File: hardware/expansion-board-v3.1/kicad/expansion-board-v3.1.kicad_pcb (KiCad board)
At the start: 6 copper layers, 100 x 62 mm, 156 parts, among them J1 PinHeader_2x20_P2.54mm_Vertic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, J2 U.FL_Hirose_U.FL-R-SMT-1_Vert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, J4 USB_C_Receptacle_HRO_TYPE-C-3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, J5 U.FL_Hirose_U.FL-R-SMT-1_Vert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, J6 U.FL_Hirose_U.FL-R-SMT-1_Vert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, J8 U.FL_Hirose_U.FL-R-SMT-1_Vert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, Q2 SOT-23, Q3 SOT-23, Q4 SOT-23, Q5 SOT-23, SW1 SolderJumper-2_P1.3mm_Open_Pa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, SW2 SolderJumper-2_P1.3mm_Open_Pa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, U1 SOT-23-5, U10 QFN-48-1EP_7x7mm_P0.5mm_EP5.1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, U11 DFN-8-1EP_2x2mm_P0.5mm_EP0.86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, U12 SOT-363_SC-70-6, U13 AD8319_LFCSP-8-EP, U14 MSOP-8_3x3mm_P0.65mm, U15 SOT-23-6, U16 SOT-363_SC-70-6, U17 SOT-363_SC-70-6, U2 SOT-23-5, U3 SOT-23-5, U4 BNO085_LGA-28, U5 BMP388_LGA-10, U6 LGA-16_3x3mm_P0.5mm, U7 ATGM336H_LCC-18, U8 QFN-56-1EP_7x7mm_P0.4mm_EP3.2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, U9 SOIC-8_5.3x5.3mm_P1.27mm, Y1 Crystal_SMD_3225-4Pin_3.2x2.5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, Y2 Crystal_SMD_3225-4Pin_3.2x2.5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, Y3 Crystal_SMD_3215-2Pin_3.2x1.5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

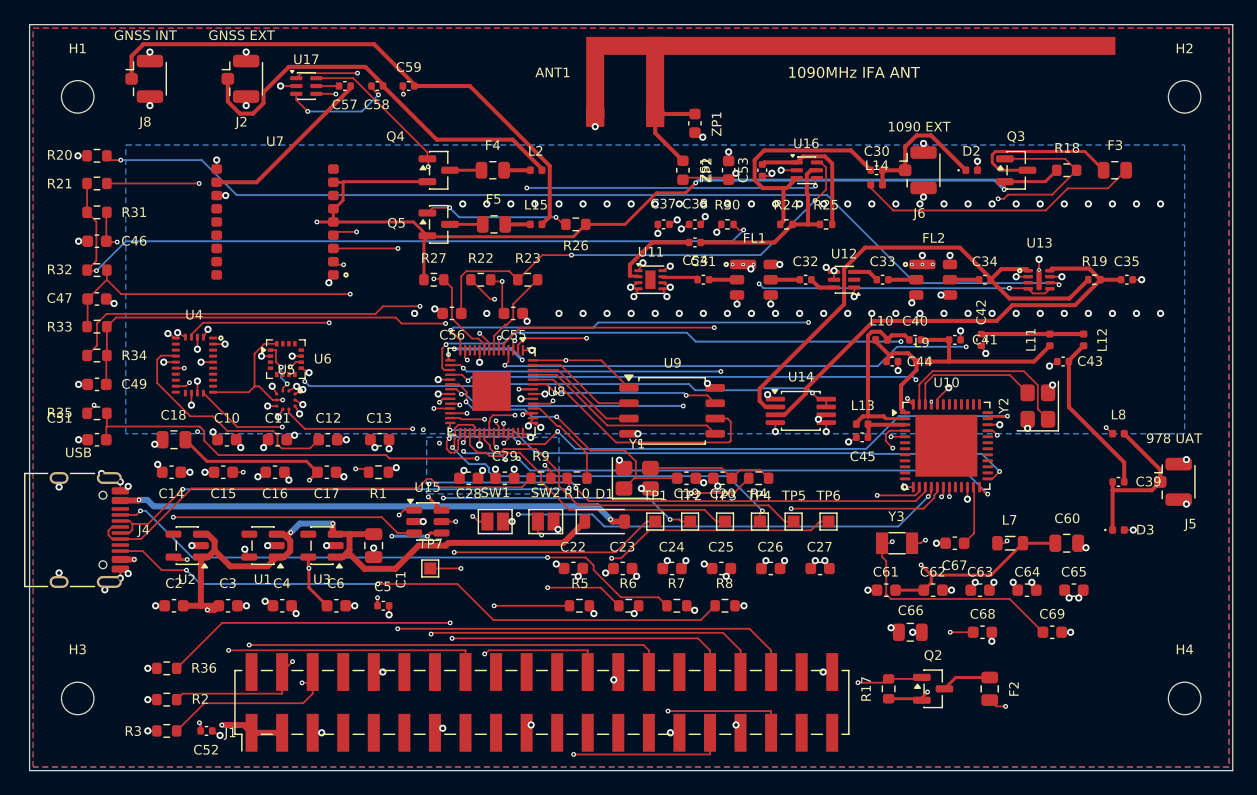
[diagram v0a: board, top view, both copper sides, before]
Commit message: feat(hw): EP 散热过孔 8→54 个 —— 挡路的一半是内层走线，另一半是我把锡膏当成了铜
评审质疑"U8/U10 是板上最大的芯片，打 4、5 个孔都没问题"。**他是对的，而且
我上一版给出的理由只对了一半。** 两个独立原因叠在一起：

## 真因①：内层走线从 EP 底下横穿（已修，export_dsn 加 EP keepout）

散热过孔是**通孔，穿透全部 6 层**，而之前从没给 EP 在内层留过地方。
freerouting 于是把 In2/B.Cu 的线直接从 EP 底下穿过去。

修法与射频 keepout 同一机制：EP 焊盘 bbox 外扩 0.05mm，在 **In2/B.Cu 生成禁布区**。
不锁 F.Cu——EP 四周的引脚要在顶层扇出，锁了等于把芯片封死；In1/In3/In4 是平面层，
本来就不布线。实测 U10 EP 底下的内层走线：5 条 In2 + 3 条 B.Cu → **0 条**。

## 真因②：QFN 的 F.Paste 锡膏分格被当成了铜障碍（这条是我的 bug）

清掉内层走线后**依然一个孔都打不下**。挖下去才发现，挡路的是这些东西：

    U10 pad num='' net='' pos=(124.27,83.06) size=1.04x1.04 layers=['F.Paste']
                                                            ~~~~~~~~~~~~~~~~~

QFN 的 EP 在封装里被切成 4×4 个锡膏方块（钢网开窗，标准做法）。它们 net 为空、
不等于 "GND"，于是 thermal_vias 把它们当成非 GND 障碍，报 EP 正中央"缺 0.173mm"
—— 那 0.173 正好是锡膏格之间的缝宽。**锡膏不是铜，压根不挡过孔。**

我上一版拿这个 0.177mm 的实测值当证据，断言"内层走线把 EP 切成 0.35mm 小格"。
量到的数是真的，归因是错的：那个距离根本不是走线给的。
判据改用 `pad.IsOnCopperLayer()`（LSET 不支持 `&` 运算符）。U10 实测 49 铜 / 16 锡膏格。

**教训**：焊盘不等于铜。凡是拿 pad 做几何判断的地方，都得先问它在哪一层——
本仓 stitch_gnd.py 有同样的写法，暂未走流程，留待它启用时一并修。

## 结果

    U10  0 → 33 个      U8   0 → 11 个      U11  0 → 1 个
    U13  2 → 3 个       FL1/FL2 各 3 个     合计 8 → 54 个

## 顺带

- 名单抽到 ep_targets.py，export_dsn 与 thermal_vias 共用。分叉的话症状是隐性的
  （DRC 全绿、只是孔数偏少），很难发现。
- 整条链固化成 tools/run_route.sh。之前靠手敲 8 步命令，跑到第 5 步才发现第 2 步
  用的是上一版板子，这种事出过不止一次。踩到两个环境坑，都写进脚本注释了：
  freerouting 2.2.4 要 **Java 25**（本机唯一的 25 在 ServBay 里，java_home 找不到），
  kicad-cli 在 **~/Applications** 不是 /Applications。
- 固化这次的手工调整：Q3 转向 0° → 180°（其余元件未动）。

## 代价，需要人工知道

未连通 **3 → 8**。EP keepout 占掉了内层通道，freerouting 得绕路。
新增的 5 处：3V3_RF ×2、RP_1V1 ×3（都是 via↔track / zone↔zone 这类覆铜断口），
外加老面孔 SUBG_IRQ、SUBG_VDDR 仍未解决。铜层 DRC 仅剩 1 项 starved_thermal（非致命）。

试过 ripup_retry 拆 SUBG_RESET/SUBG_SYNC/SUBG_X48N 给它们让路：未连通 8→11
且引入 1 条 clearance，**不赚，已按该工具自己的判据回退**。
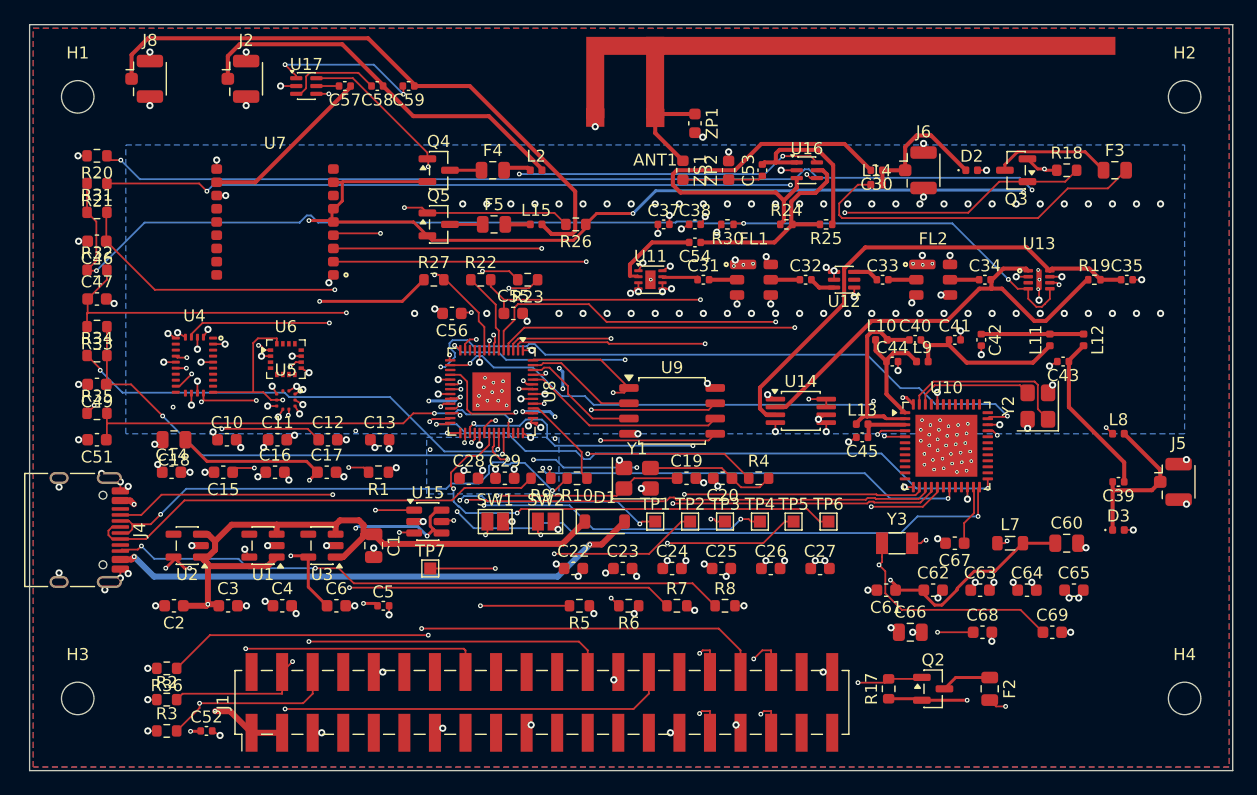
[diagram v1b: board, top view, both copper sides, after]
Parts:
- turned Q3 to 180 degrees
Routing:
- net SUBG_IRQ: track 56.5 -> 0.00 mm, vias 3 -> 0
- net DEMOD3: track 54.4 -> 39.7 mm
- net SW1_J2: track 19.6 -> 33.5 mm
- net 3V3_GNSS: track 175.4 -> 187.7 mm, vias 6 -> 8
- net BIAS_EN_1090: track 67.7 -> 56.9 mm, vias 3 -> 2
- net SUBG_TMSC: track 48.6 -> 57.7 mm
- net 3V3_RF: track 54.6 -> 63.2 mm
- net SUBG_RESET: track 54.2 -> 60.6 mm, vias 4 -> 3
- net RF1090_FEED: track 23.6 -> 29.8 mm
- net BIAS_EN_978: track 58.5 -> 64.7 mm
- net IMU_INT: track 60.3 -> 65.9 mm
- net DET_IN: track 42.4 -> 36.9 mm
- net AD8313_VOUT: track 72.6 -> 77.9 mm
- net SWCLK: track 31.7 -> 26.9 mm, vias 2 -> 3
- net ANT_GNSS_INT: track 46.4 -> 51.3 mm
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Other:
- board text removed: "(c) Pilot Kit"
- board text removed: "1090 / 978 ADS-B + GNSS + IMU + BARO"
- board text removed: "1090 EXT"
- board text removed: "1090MHz IFA ANT"
- board text removed: "978 UAT"
- board text removed: "GNSS EXT"
- board text removed: "GNSS INT"
- board text removed: "Pilot Kit Avionics Board"
- board text removed: "USB"
- board text removed: "V1 2026-08"
- board text removed: "https://air.club"

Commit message: fix(hw): route_fix 三个错判 —— 真缺线被当碎铜、过孔尺寸写死、障碍过孔按常量算
未连通 8 → 5，铜层 DRC 回到 0 致命项（仅剩 1 项 starved_thermal 非致命）。
三个 bug 是查上一条 commit 留下的"未连通 3→8"时挖出来的，彼此独立。

## ① 真缺线被误判成"孤立碎铜"，永远没人去布

load_jobs 原来的分类判据是「DRC 报的两端里有没有 Pad」：

    (need if "Pad" in kinds else orphan).append(...)

于是 Track↔Track、Via↔Track 一律归为 orphan（该删的断头铜）。
实测漏判：**3V3_RF 有两处缺口跨 26mm 和 10.7mm**，两端各自都连着一大片铜和
焊盘——那是"两大块该连没连"，不是碎铜。被归错类的后果有两层：没人去布它，
而且差点被 clean 当垃圾删掉。

改判据为「两端所在的**连通块是否各自都含焊盘**」。都含 → 真缺线；
有一端不含 → 那端确实没接上任何东西，交给 clean。
改完立刻多认出 4 处可布的，其中 3 处一次就布通了。

## ② 过孔尺寸写死 0.6/0.3，而复核按常量 0.4 算

    v.SetWidth(pcbnew.FromMM(0.6))      ← 落盘
    VIA_R = 0.20                        ← 复核用的常量（盘 0.4）

上一轮把常量同步板规改成 0.4/0.2 时**只改了常量，漏了落盘这两行**。
后果很隐蔽：净空复核按盘 0.4 算说余量 +0.058mm，实际却往板里塞盘 0.6，
KiCad 一跑就是 `actual 0.108 < 0.150`。差的 0.1mm 正好是两个半径之差。

## ③ 障碍过孔一律按 VIA_R 常量算半径

板上过孔根本不是一种尺寸：GND 缝合过孔盘 0.6、散热过孔盘 0.3、本模块布的 0.4。
snap_obstacles 把它们统统当 0.2 半径，遇上 0.6 的就低估 0.1mm，
于是又漏过一条 `actual 0.105 < 0.150`。改成读 `t.GetWidth()/2` 实际值。

修完之后复核开始正常工作了——它主动弃用了两条会违规的走线
（"⚠️ 几何复核不过，弃用"），宁可少布一条也不往板子里塞 DRC 违例。

**教训**：②③ 加上前面的封装禁铜层、gen_pcb 板规下限，是同一族问题的第 3、4 次：
**改了一个尺寸/层数，散落各处写死的副本没跟着改**。而且症状全都不是报错，
是"复核通过了但板子是错的"。

## 剩余 5 处未连通（未解决，需要评审定夺）

    SUBG_IRQ    U8.17 ↔ U10.18，跨 42mm，freerouting 和 route_fix 都布不通
    SUBG_VDDR   U10.45，老面孔（via-in-pad 那处）
    RP_1V1  ×2  覆铜岛断口
    I2C_SCL     U5.2 的 stub 末端到 In2 差 1.47mm + 一个过孔

其中 I2C_SCL 每轮都被 route_fix 判成"✅ 0 段 0 过孔（1 节点）"——它认为已经
连通，而 DRC 说没有，然后 clean 又把那段删掉，来回死循环。这是第 4 个错判，
还没修。

试过 ripup_retry 给 SUBG_IRQ/SUBG_VDDR 让路（拆 SUBG_RESET/SUBG_SYNC/SUBG_X48N）：
未连通 8→11 且引入 clearance，不赚，已回退。
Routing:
- net 3V3_RF: track 63.2 -> 74.0 mm
- net RP_1V1: track 25.7 -> 36.0 mm, vias 11 -> 12
- net I2C_SCL: track 51.6 -> 52.2 mm
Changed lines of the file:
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@@
 	)
 	(segment
+		(start 118.6 75.1)
+		(end 112.75 80.95)
+		(width 0.25)
+		(layer "F.Cu")
+		(net "3V3_RF")
+	)
+	(segment
 		(start 77.7505 98.1024)
 		(end 78.7224 98.1024)
@@
 	)
 	(segment
+		(start 118.6 72.55)
+		(end 118.6 75.1)
+		(width 0.25)
+		(layer "F.Cu")
+		(net "3V3_RF")
+	)
+	(segment
 		(start 83.8736 92.25)
 		(end 83.5813 91.9576)
@@
 	)
 	(segment
+		(start 71.05 80.4375)
+		(end 71.05 79.85)
+		(width 0.15)
+		(layer "F.Cu")
+		(net "I2C_SCL")
+	)
+	(segment
 		(start 64.45 81.2368)
 		(end 68.8427 81.2368)
@@
 	)
 	(segment
+		(start 83.5 85.3)
+		(end 83.35 85.3)
+		(width 0.25)
+		(layer "F.Cu")
+		(net "RP_1V1")
+	)
+	(segment
 		(start 90.9872 82.2754)
 		(end 91.8129 82.2754)
@@
 	)
 	(segment
+		(start 84.85 86.65)
+		(end 83.5 85.3)
+		(width 0.25)
+		(layer "F.Cu")
+		(net "RP_1V1")
+	)
+	(segment
 		(start 84.9871 81.0754)
 		(end 84.9625 81.1)
@@
 	)
 	(via
+		(at 84.85 86.65)
+		(size 0.4)
+		(drill 0.2)
+		(layers "F.Cu" "B.Cu")
+		(net "RP_1V1")
+	)
+	(via
 		(at 93.6769 84.4061)
 		(size 0.4)
@@
 	)
 	(segment
+		(start 89.35 78.85)
+		(end 87.55 78.85)
+		(width 0.25)
+		(layer "B.Cu")
+		(net "RP_1V1")
+	)
+	(segment
 		(start 85.3514 81.2767)
 		(end 85.6813 80.9468)
@@
 	)
 	(segment
+		(start 87.55 78.85)
+		(end 86.35 80.05)
+		(width 0.25)
+		(layer "B.Cu")
+		(net "RP_1V1")
+	)
+	(segment
+		(start 86.35 80.05)
+		(end 86.35 80.5)
+		(width 0.25)
+		(layer "B.Cu")
+		(net "RP_1V1")
+	)
+	(segment
 		(start 94.3205 78.8586)
 		(end 94.3205 80.261)
@@
 	)
 	(segment
+		(start 86.35 80.5)
+		(end 85.9 80.95)
+		(width 0.25)
+		(layer "B.Cu")
+		(net "RP_1V1")
+	)
+	(segment
+		(start 85.9 80.95)
+		(end 85.75 80.95)
+		(width 0.25)
+		(layer "B.Cu")
+		(net "RP_1V1")
+	)
+	(segment
+		(start 90.7 80.2)
+		(end 89.35 78.85)
+		(width 0.25)
+		(layer "B.Cu")
+		(net "RP_1V1")
+	)
+	(segment
 		(start 83.1801 81.2767)
 		(end 85.3514 81.2767)
@@
 	)
 	(segment
+		(start 85.6 86.65)
+		(end 84.85 86.65)
+		(width 0.25)
+		(layer "B.Cu")
+		(net "RP_1V1")
+	)
+	(segment
+		(start 86.05 87.1)
+		(end 85.6 86.65)
+		(width 0.25)
+		(layer "B.Cu")
+		(net "RP_1V1")
+	)
+	(segment
 		(start 94.0233 78.5614)
 		(end 94.3205 78.8586)
@@
 		(width 0.25)
 		(layer "B.Cu")
+		(net "RP_1V1")
+	)
+	(segment
+		(start 90.7 80.35)
+		(end 90.7 80.2)
+		(width 0.25)
+		(layer "B.Cu")

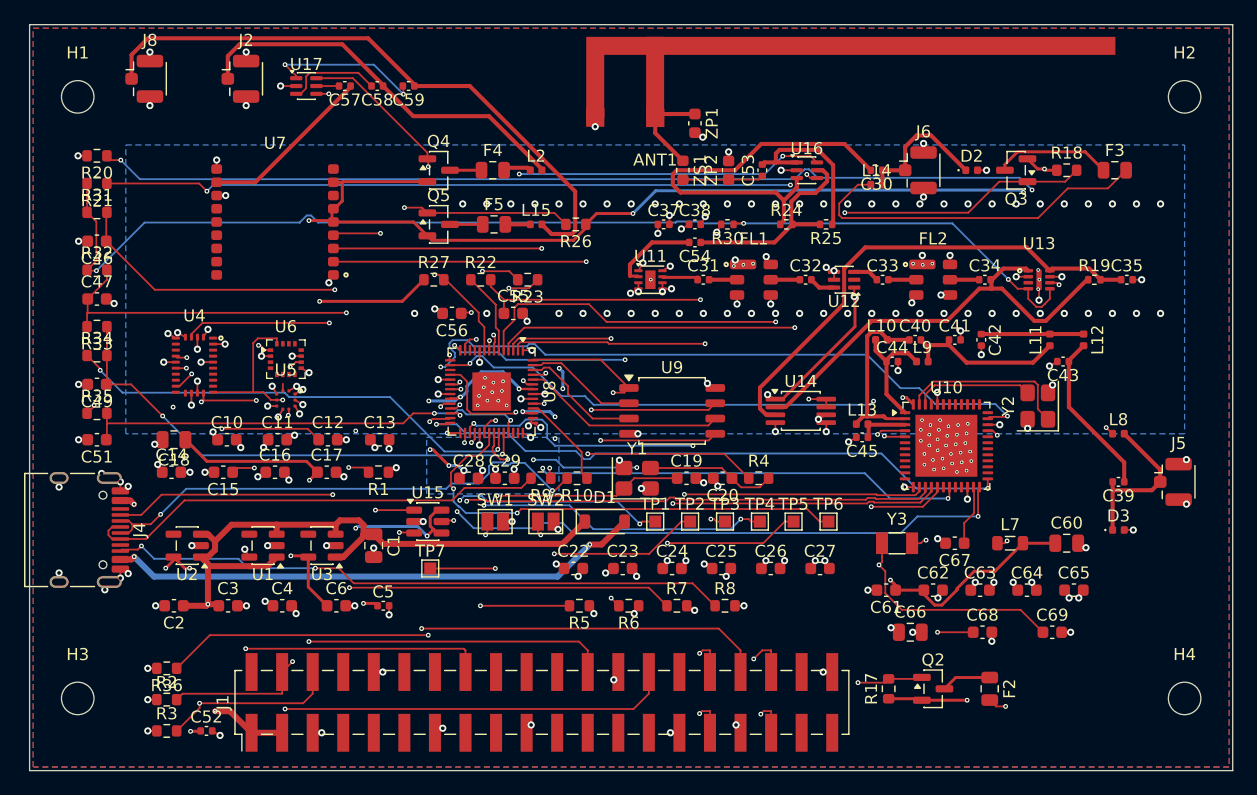
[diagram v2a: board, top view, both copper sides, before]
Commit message: fix(hw): EP 禁布区按孔阵反算而非整块铺 —— 未连通 5→2，铜层 DRC 归零
评审提问"几个 U 的禁布需要这么大面积吗"。**不需要，我没论证过就按整个 EP 铺了。**
查了业界通行做法（Microchip AN4498 / Infineon AN72845 / TI SLOA122 口径一致）：

    QFN 的 EP 用 9–25 个 Ø0.3–0.33mm 孔，间距 1.0–1.2mm

而我打的是 U10 **33 个、间距 0.8mm** —— 孔数超上限、间距也比推荐密。
0.8mm 是"物理上最密能排多少"，不是"该排多少"。热需求这边：CC1312R 发射态
约 82mW、RP2040 满载约 100mW，这个量级下 16 个孔和 33 个孔的热阻差别没有工程
意义；密排反而在回流焊时抢锡、加大空洞率。

## 改法：禁布区按孔阵实际占的中心区反算

孔数在 ep_targets.EP_VIAS 定死（U8 9 个 3×3 / U10 16 个 4×4），间距 1.2mm，
export_dsn 和 thermal_vias 共用这一份反算各自的几何：

    U10   EP 5.15×5.15   禁布 27.56 → 16.00 mm²/层   四周留 0.58mm 环带给内层
    U8    EP 3.20×3.20   禁布 10.89 →  7.84 mm²/层   四周留 0.20mm
    合计               45.2 → 30.6 mm²/层（省 32%）

0.58mm 环带够过一条 0.15mm 线（净空 0.15+线 0.15+净空 0.15 = 0.45）。
走线在 In2 从 EP 下方过不影响电气——叠层 F/In1(GND)/In2/In3/In4(GND)/B，
EP 与 In2 之间隔着 In1 整块地平面。

## 两个回归，一并修掉

- **FL1/FL2 掉到 1 个孔**。1.2mm 间距在 2.2×0.8 的长地焊盘上只塞得下 1 个，
  而 LAYOUT_CONSTRAINTS §2.4 明确要求 ≥3 个。小 EP 的孔作用是**射频地回流**
  不是散热，密排本来就对——改成大 EP 用 1.2mm、小 EP 仍用 0.8mm 两档。
- **U10 只放到 13/16、U8 7/9**。贪心细扫按"离中心最近"取点，排不出规则格阵，
  空位被环带走线蹭掉。大 EP 改走**规则阵列**：keepout 已经保证中心区干净，
  规则排必然排得下（保留 hole_ok 兜底，排不下会打印警告）。

## 结果 —— 全项目历史最好

    未连通       5 → 2      （EP keepout 之前的基线是 3）
    铜层 DRC     1 → 0 违例
    孤立断头铜   → 0
    散热过孔     34 个，目标全部达成：U10 16/16、U8 9/9、FL1/FL2 各 3(§2.4 达标)
    射频         160 段全 F.Cu、0 过孔

省出来的内层通道确实兑现了：In2 走线 254 → 282 段。

剩 2 处未连通：SUBG_VDDR(U10.45) 和 RP_1V1(U8.23)，都是老面孔。
route_fix 收不动；ripup_retry 拆 3V3_DIG/SWCLK/SUBG_X48N 让路试过，
未连通 2→3 还带 3 条 dangling，不赚，已回退。这两处多半要靠挪元件。
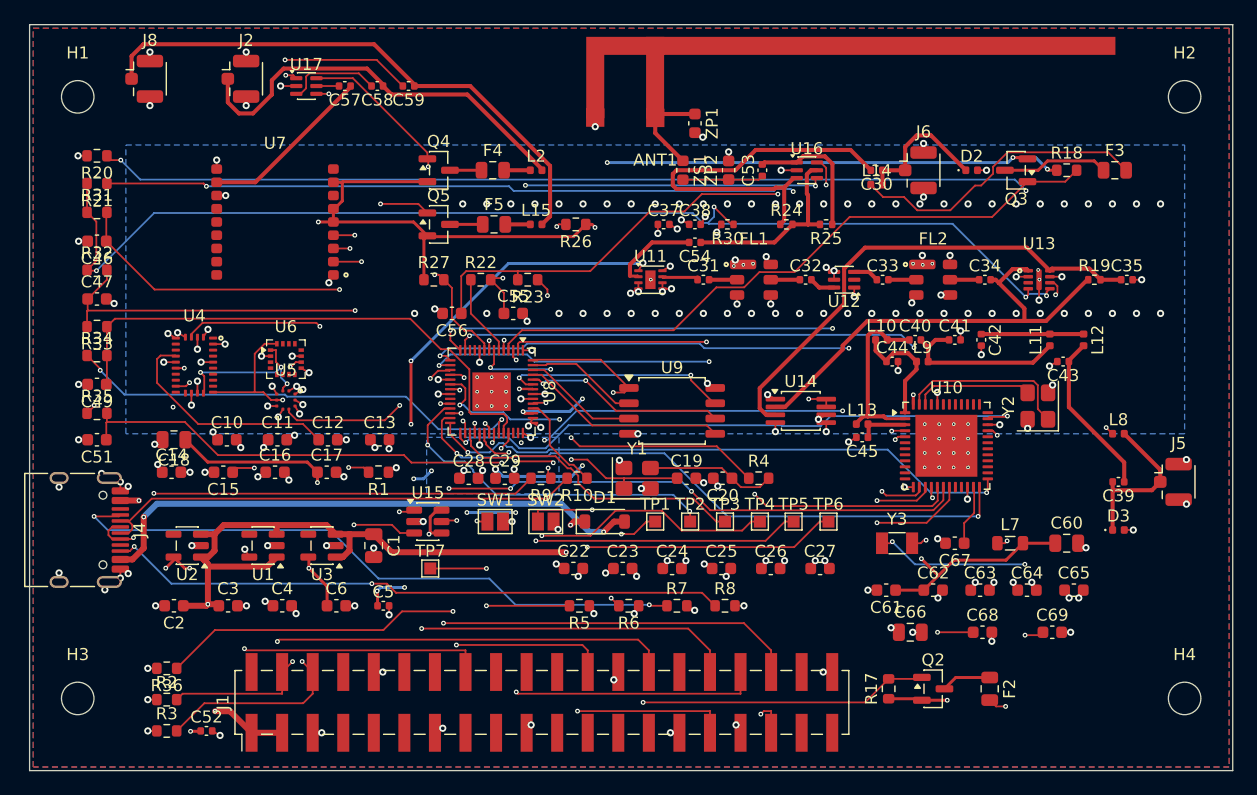
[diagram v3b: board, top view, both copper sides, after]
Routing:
- net SUBG_IRQ: track 0.00 -> 55.5 mm, vias 0 -> 4
- net 3V3_RF: track 74.0 -> 92.3 mm, vias 16 -> 19
- net SWCLK: track 26.9 -> 41.4 mm, vias 3 -> 2
- net SUBG_RESET: track 60.6 -> 49.5 mm, vias 3 -> 2
- net SUBG_SYNC: track 49.6 -> 58.2 mm, vias 3 -> 4
- net IMU_INT: track 65.9 -> 58.9 mm
- net ANT_SEL_1090_B: track 8.44 -> 14.5 mm, vias 2 -> 3
- net SUBG_TMSC: track 57.7 -> 52.3 mm, vias 3 -> 2
- net RF1090_FEED: track 29.8 -> 25.1 mm
- net ANT_GNSS_INT: track 51.3 -> 46.5 mm
- net BIAS_EN_978: track 64.7 -> 60.2 mm
- net SUBG_MOSI: track 48.6 -> 53.0 mm
- net SUBG_X32K1: track 31.0 -> 27.1 mm
- net 3V3_GNSS: track 187.7 -> 183.8 mm
- net SUBG_SCK: track 49.0 -> 52.8 mm, vias 2 -> 3
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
